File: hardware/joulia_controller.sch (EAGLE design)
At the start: 41 parts, among them IC1 LM2902D, IC2 LM2902D, U1 MMBT2222ALT1G, U2 MMBT2222ALT1G

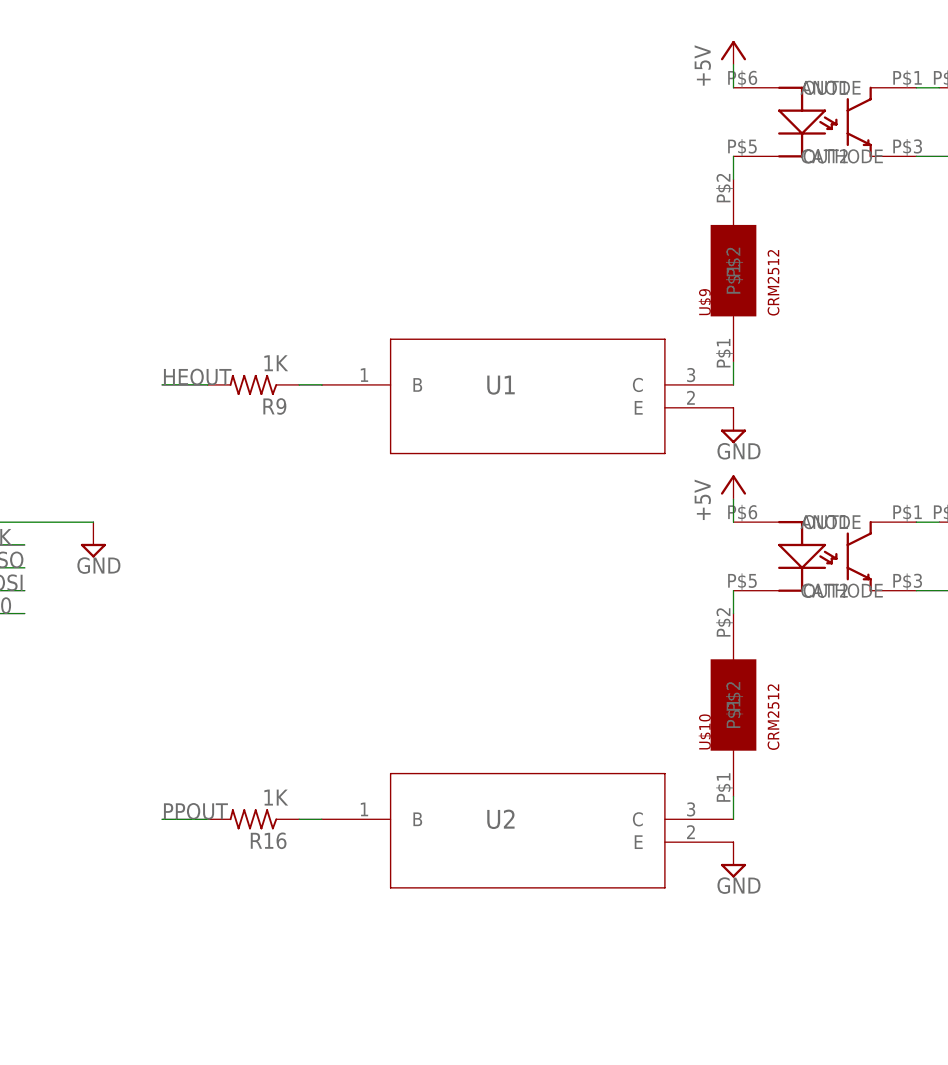
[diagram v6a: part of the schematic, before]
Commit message: Using smaller resistor for optoisolator emitter.
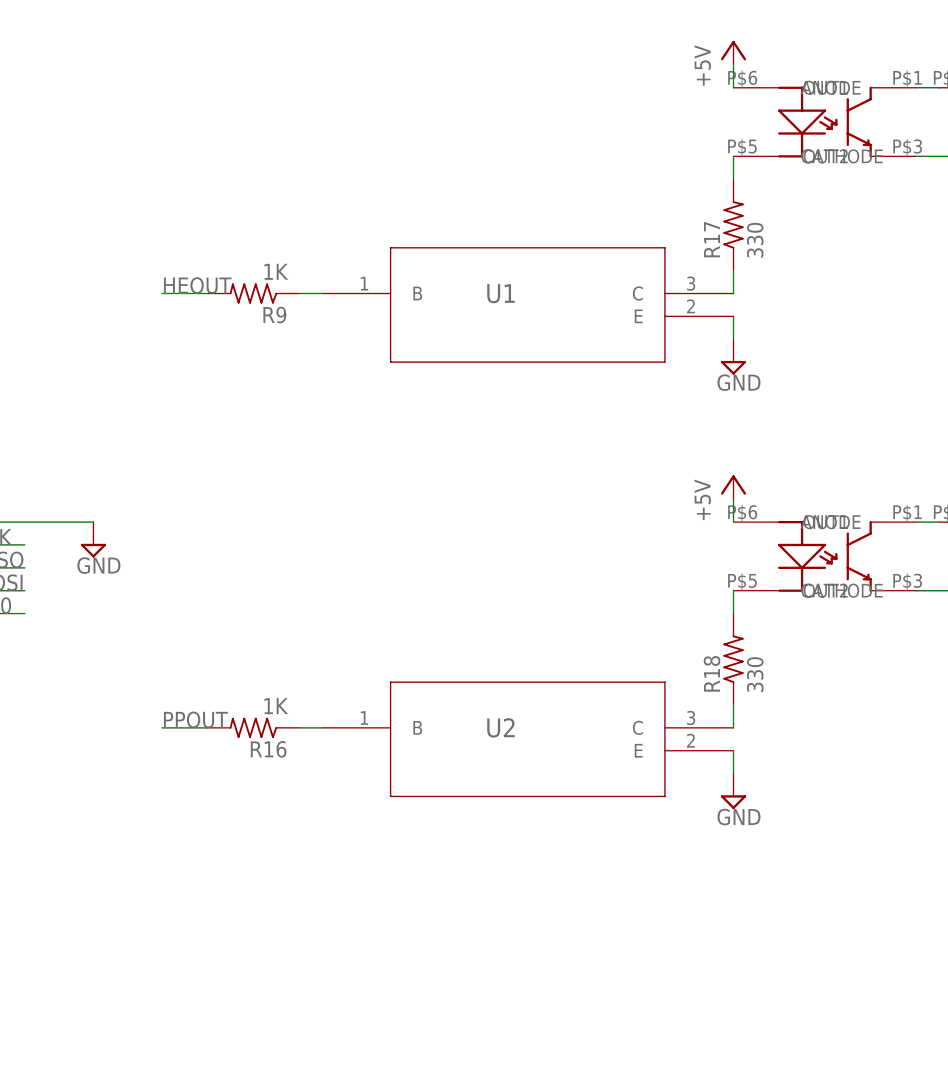
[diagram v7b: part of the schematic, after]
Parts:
- removed U$10, U$9: CRM2512, digikey:CRM2512
- added R17, R18: 330, resistor:R-US_R1206
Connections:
- net N$13: now also R17.1; no longer U$9.P$1
- net N$14: now also R17.2; no longer U$9.P$2
- net N$17: now also R18.2; no longer U$10.P$2
- net N$18: now also R18.1; no longer U$10.P$1
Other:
- moved on the sheet: R16, R9, U1, U2
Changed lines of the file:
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@@
 <part name="SUPPLY17" library="supply2" library_urn="urn:adsk.eagle:library:372" deviceset="GND" device=""/>
 <part name="SUPPLY18" library="supply2" library_urn="urn:adsk.eagle:library:372" deviceset="GND" device=""/>
-<part name="U$9" library="digikey" deviceset="CRM2512" device=""/>
-<part name="U$10" library="digikey" deviceset="CRM2512" device=""/>
 <part name="V240" library="digikey" deviceset="PC1720589" device=""/>
 <part name="V120" library="digikey" deviceset="PC1720589" device=""/>
 <part name="SUPPLY19" library="supply2" library_urn="urn:adsk.eagle:library:372" deviceset="GND" device=""/>
+<part name="R17" library="resistor" library_urn="urn:adsk.eagle:library:348" deviceset="R-US_" device="R1206" value="330"/>
+<part name="R18" library="resistor" library_urn="urn:adsk.eagle:library:348" deviceset="R-US_" device="R1206" value="330"/>
 </parts>
 <sheets>
@@
 <instance part="SUPPLY8" gate="GND" x="-15.24" y="104.14"/>
 <instance part="SUPPLY9" gate="GND" x="-10.16" y="40.64"/>
-<instance part="U1" gate="A" x="198.12" y="93.98"/>
-<instance part="U2" gate="A" x="198.12" y="45.72"/>
-<instance part="SUPPLY10" gate="GND" x="243.84" y="40.64"/>
-<instance part="SUPPLY11" gate="GND" x="243.84" y="88.9"/>
+<instance part="U1" gate="A" x="198.12" y="104.14"/>
+<instance part="U2" gate="A" x="198.12" y="55.88"/>
+<instance part="SUPPLY10" gate="GND" x="243.84" y="48.26"/>
+<instance part="SUPPLY11" gate="GND" x="243.84" y="96.52"/>
 <instance part="PWR" gate="A" x="-76.2" y="30.48"/>
 <instance part="P+3" gate="1" x="-71.12" y="40.64"/>
@@
 <instance part="SUPPLY15" gate="GND" x="50.8" y="81.28"/>
 <instance part="SUPPLY16" gate="GND" x="50.8" y="17.78"/>
-<instance part="R9" gate="G$1" x="190.5" y="93.98" rot="R180"/>
-<instance part="R16" gate="G$1" x="190.5" y="45.72" rot="R180"/>
+<instance part="R9" gate="G$1" x="190.5" y="104.14" rot="R180"/>
+<instance part="R16" gate="G$1" x="190.5" y="55.88" rot="R180"/>
 <instance part="U$1" gate="G$1" x="292.1" y="124.46"/>
 <instance part="U$2" gate="G$1" x="292.1" y="76.2"/>
@@
 <instance part="SUPPLY17" gate="GND" x="322.58" y="119.38"/>
 <instance part="SUPPLY18" gate="GND" x="322.58" y="71.12"/>
-<instance part="U$9" gate="G$1" x="243.84" y="106.68" rot="R90"/>
-<instance part="U$10" gate="G$1" x="243.84" y="58.42" rot="R90"/>
 <instance part="V240" gate="G$1" x="332.74" y="106.68"/>
 <instance part="V120" gate="G$1" x="332.74" y="55.88"/>
 <instance part="SUPPLY19" gate="GND" x="327.66" y="111.76" rot="R180"/>
+<instance part="R17" gate="G$1" x="243.84" y="111.76" rot="R90"/>
+<instance part="R18" gate="G$1" x="243.84" y="63.5" rot="R90"/>
 </instances>
 <busses>
@@
 <pinref part="U1" gate="A" pin="E"/>
 <pinref part="SUPPLY11" gate="GND" pin="GND"/>
+<wire x1="243.84" y1="99.06" x2="243.84" y2="101.6" width="0.1524" layer="91"/>
 </segment>
 <segment>
 <pinref part="U2" gate="A" pin="E"/>
 <pinref part="SUPPLY10" gate="GND" pin="GND"/>
+<wire x1="243.84" y1="50.8" x2="243.84" y2="53.34" width="0.1524" layer="91"/>
 </segment>
 <segment>
@@
 <segment>
 <pinref part="R9" gate="G$1" pin="2"/>
-<label x="180.34" y="93.98" size="1.778" layer="95"/>
-<wire x1="185.42" y1="93.98" x2="180.34" y2="93.98" width="0.1524" layer="91"/>
+<label x="180.34" y="104.14" size="1.778" layer="95"/>
+<wire x1="185.42" y1="104.14" x2="180.34" y2="104.14" width="0.1524" layer="91"/>
 </segment>
 </net>
@@
 <segment>
 <pinref part="R16" gate="G$1" pin="2"/>
-<label x="180.34" y="45.72" size="1.778" layer="95"/>
-<wire x1="185.42" y1="45.72" x2="180.34" y2="45.72" width="0.1524" layer="91"/>
+<label x="180.34" y="55.88" size="1.778" layer="95"/>
+<wire x1="185.42" y1="55.88" x2="180.34" y2="55.88" width="0.1524" layer="91"/>
 </segment>
 </net>
@@
 <pinref part="U1" gate="A" pin="B"/>
 <pinref part="R9" gate="G$1" pin="1"/>
-<wire x1="195.58" y1="93.98" x2="198.12" y2="93.98" width="0.1524" layer="91"/>
+<wire x1="195.58" y1="104.14" x2="198.12" y2="104.14" width="0.1524" layer="91"/>
 </segment>
 </net>
@@
 <pinref part="U2" gate="A" pin="B"/>
 <pinref part="R16" gate="G$1" pin="1"/>
-<wire x1="195.58" y1="45.72" x2="198.12" y2="45.72" width="0.1524" layer="91"/>
+<wire x1="195.58" y1="55.88" x2="198.12" y2="55.88" width="0.1524" layer="91"/>
 </segment>
 </net>
@@
 </segment>
 </net>
-<net name="N$13" class="1">
+<net name="N$13" class="0">
 <segment>
 <pinref part="U1" gate="A" pin="C"/>
-<pinref part="U$9" gate="G$1" pin="P$1"/>
-<wire x1="243.84" y1="93.98" x2="243.84" y2="96.52" width="0.1524" layer="91"/>
-</segment>
-</net>
-<net name="N$14" class="1">
+<wire x1="243.84" y1="104.14" x2="243.84" y2="106.68" width="0.1524" layer="91"/>
+<pinref part="R17" gate="G$1" pin="1"/>
+</segment>
+</net>
+<net name="N$14" class="0">
 <segment>
 <pinref part="U$5" gate="G$1" pin="CATHODE"/>
-<pinref part="U$9" gate="G$1" pin="P$2"/>
 <wire x1="243.84" y1="116.84" x2="243.84" y2="119.38" width="0.1524" layer="91"/>
-</segment>
-</net>
-<net name="N$17" class="1">
+<pinref part="R17" gate="G$1" pin="2"/>
+</segment>
+</net>
+<net name="N$17" class="0">
 <segment>
 <pinref part="U$6" gate="G$1" pin="CATHODE"/>
-<pinref part="U$10" gate="G$1" pin="P$2"/>
 <wire x1="243.84" y1="68.58" x2="243.84" y2="71.12" width="0.1524" layer="91"/>
-</segment>
-</net>
-<net name="N$18" class="1">
-<segment>
-<pinref part="U$10" gate="G$1" pin="P$1"/>
+<pinref part="R18" gate="G$1" pin="2"/>
+</segment>
+</net>
+<net name="N$18" class="0">
+<segment>
 <pinref part="U2" gate="A" pin="C"/>
-<wire x1="243.84" y1="45.72" x2="243.84" y2="48.26" width="0.1524" layer="91"/>
-</segment>
-</net>
+<wire x1="243.84" y1="55.88" x2="243.84" y2="58.42" width="0.1524" layer="91"/>
+<pinref part="R18" gate="G$1" pin="1"/>
+</segment>
+</net>
